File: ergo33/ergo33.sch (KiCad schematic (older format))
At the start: 112 parts, among them SW1 SW_Push, SW46 Rotary_Encoder_Switch, U1 ATmega32U4-AU, U2 USBLC6-2SC6, Y1 16MHz

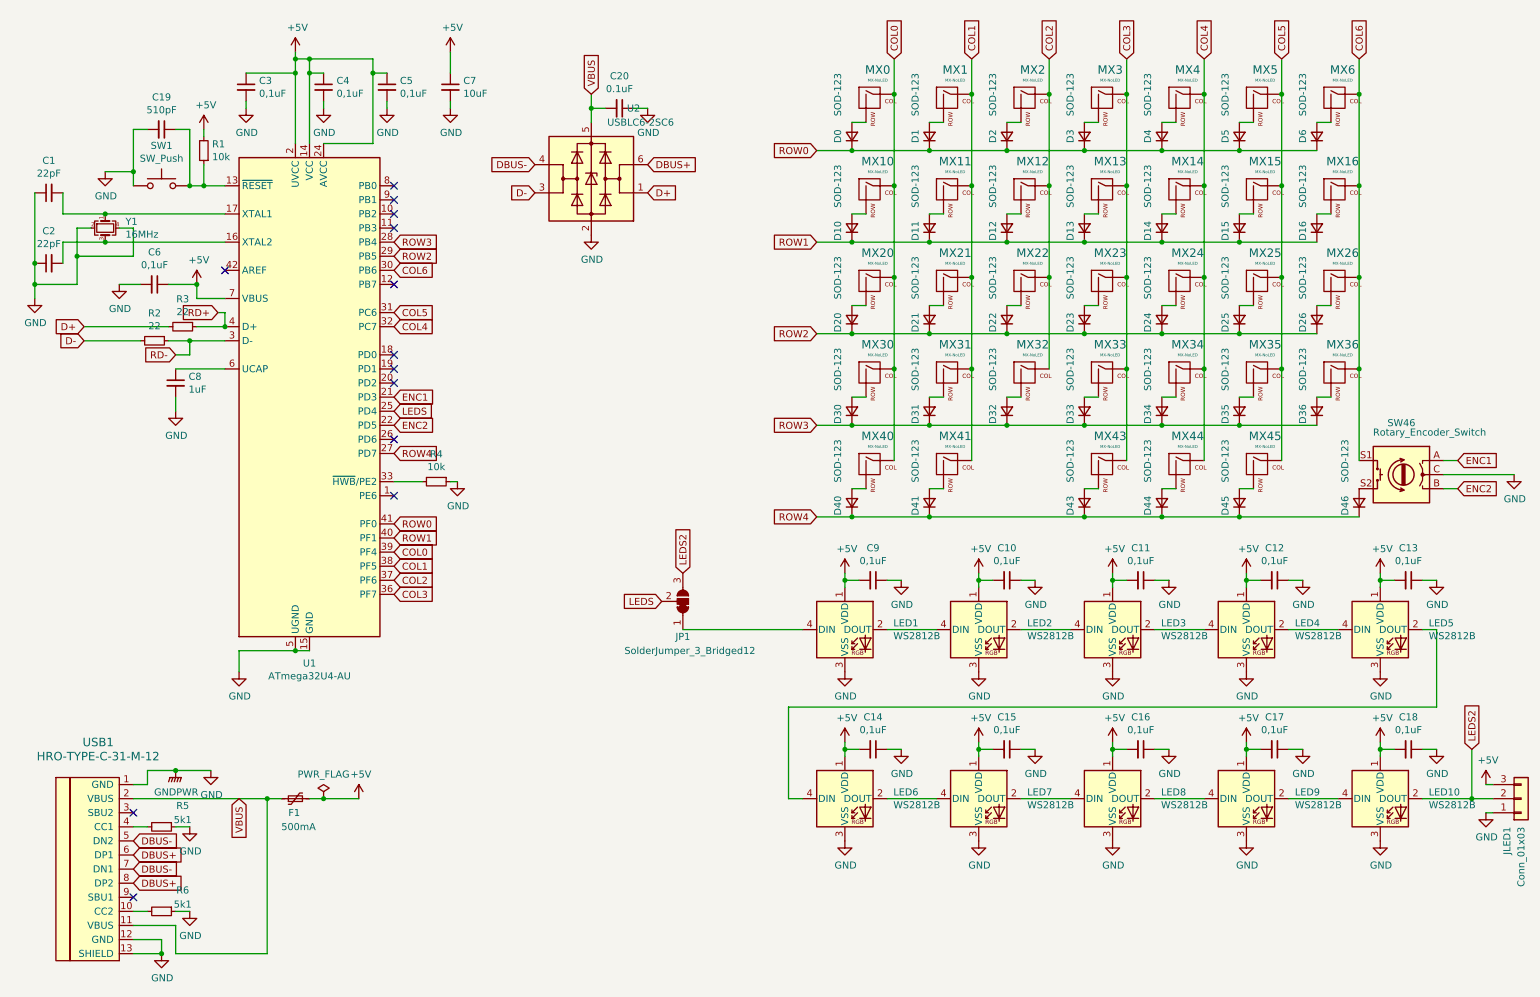
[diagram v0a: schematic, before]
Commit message: Change a few cap values
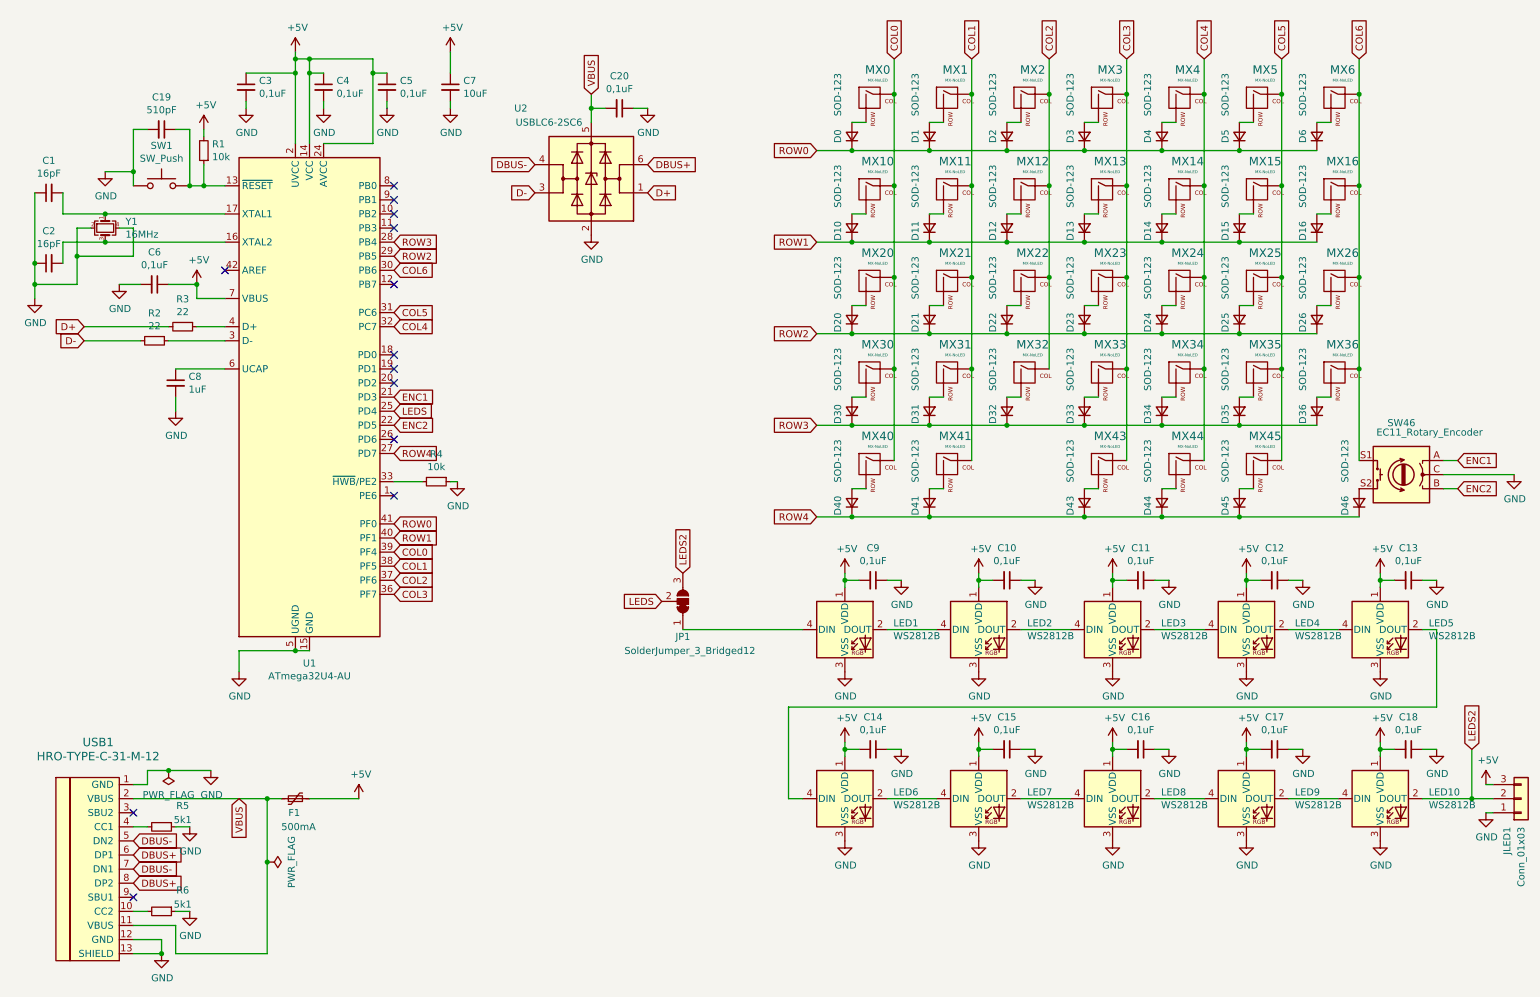
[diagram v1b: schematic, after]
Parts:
- C1, C2: value 22pF -> 16pF
- C20: value 0.1uF -> 0,1uF
- F1: Component (none) -> Littelfuse 1206L050/15
- MX0: Component (none) -> Kailh 1511 PCB socket
- SW46: value Rotary_Encoder_Switch -> EC11_Rotary_Encoder
- Y1: Component (none) -> DSX321G
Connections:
- net RD+: no longer names the net of R3.1, U1.4 (D+)
- net RD-: no longer names the net of R2.1, U1.3 (D-)
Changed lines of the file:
@@
 F 2 "Crystal:Crystal_SMD_3225-4Pin_3.2x2.5mm_HandSoldering" H 1100 2000 50  0001 C CNN
 F 3 "~" H 1100 2000 50  0001 C CNN
+F 4 "DSX321G" V 1100 2000 50  0001 C CNN "Component"
 	1    1100 2000
 	0    1    1    0
@@
 P 700 1750
 F 0 "C1" V 929 1750 50  0000 C CNN
-F 1 "22pF" V 838 1750 50  0000 C CNN
+F 1 "16pF" V 838 1750 50  0000 C CNN
 F 2 "Capacitor_SMD:C_0805_2012Metric_Pad1.15x1.40mm_HandSolder" H 700 1750 50  0001 C CNN
 F 3 "~" H 700 1750 50  0001 C CNN
@@
 P 700 2250
 F 0 "C2" V 929 2250 50  0000 C CNN
-F 1 "22pF" V 838 2250 50  0000 C CNN
+F 1 "16pF" V 838 2250 50  0000 C CNN
 F 2 "Capacitor_SMD:C_0805_2012Metric_Pad1.15x1.40mm_HandSolder" H 700 2250 50  0001 C CNN
 F 3 "~" H 700 2250 50  0001 C CNN
@@
 P 10300 3750
 F 0 "SW46" H 10300 4117 50  0000 C CNN
-F 1 "Rotary_Encoder_Switch" H 10100 4050 50  0000 C CNN
+F 1 "EC11_Rotary_Encoder" H 10100 4050 50  0000 C CNN
 F 2 "Rotary_Encoder:RotaryEncoder_Alps_EC11E-Switch_Vertical_H20mm" H 10150 3910 50  0001 C CNN
 F 3 "~" H 10300 4010 50  0001 C CNN
@@
 F 2 "MX_Only:MXOnly-1U-Hotswap" H 5925 1075 60  0001 C CNN
 F 3 "" H 5925 1075 60  0001 C CNN
+F 4 "Kailh 1511 PCB socket" H 6550 1100 50  0001 C CNN "Component"
 	1    6550 1100
 	1    0    0    -1
@@
 Connection ~ 1300 1600
 $Comp
-L power:GND #PWR0115
-U 1 1 5F1E9593
-P 1850 5850
-F 0 "#PWR0115" H 1850 5600 50  0001 C CNN
-F 1 "GND" H 1855 5677 50  0000 C CNN
-F 2 "" H 1850 5850 50  0001 C CNN
-F 3 "" H 1850 5850 50  0001 C CNN
-	1    1850 5850
-	1    0    0    -1
-$EndComp
-$Comp
 L power:GND #PWR0116
 U 1 1 5F1FCB7B
@@
 Connection ~ 1500 7150
 $Comp
-L power:PWR_FLAG #FLG0101
-U 1 1 5F224DEB
-P 2650 6050
-F 0 "#FLG0101" H 2650 6125 50  0001 C CNN
-F 1 "PWR_FLAG" H 2650 6223 50  0000 C CNN
-F 2 "" H 2650 6050 50  0001 C CNN
-F 3 "~" H 2650 6050 50  0001 C CNN
-	1    2650 6050
-	1    0    0    -1
-$EndComp
-$Comp
-L Device:Polyfuse_Small F1
-U 1 1 5F2261DB
-P 2450 6050
-F 0 "F1" V 2350 6100 50  0000 R CNN
-F 1 "500mA" V 2250 6150 50  0000 R CNN
-F 2 "Fuse:Fuse_1206_3216Metric_Pad1.42x1.75mm_HandSolder" H 2500 5850 50  0001 L CNN
-F 3 "~" H 2450 6050 50  0001 C CNN
-	1    2450 6050
-	0    -1   -1   0
-$EndComp
-$Comp
 L power:+5V #PWR0117
 U 1 1 5F227AE1
@@
 Wire Wire Line
 	2250 6050 2350 6050
-Wire Wire Line
-	2550 6050 2650 6050
 Connection ~ 2250 6050
 $Comp
@@
 	1600 7150 2250 7150
 Wire Wire Line
-	2250 6050 2250 7150
-Wire Wire Line
-	1300 6050 2250 6050
+	2250 6050 2250 6500
 Wire Wire Line
 	1300 5950 1400 5950
@@
 P 4750 1150
 F 0 "C20" V 4521 1150 50  0000 C CNN
-F 1 "0.1uF" V 4612 1150 50  0000 C CNN
+F 1 "0,1uF" V 4612 1150 50  0000 C CNN
 F 2 "Capacitor_SMD:C_0805_2012Metric_Pad1.15x1.40mm_HandSolder" H 4750 1150 50  0001 C CNN
 F 3 "~" H 4750 1150 50  0001 C CNN
@@
 U 1 1 5F4FCCDF
 P 4550 1650
-F 0 "U2" H 4250 2150 50  0000 C CNN
-F 1 "USBLC6-2SC6" H 4200 2050 50  0000 C CNN
+F 0 "U2" H 5050 2150 50  0000 C CNN
+F 1 "USBLC6-2SC6" H 4850 2050 50  0000 C CNN
 F 2 "Package_TO_SOT_SMD:SOT-23-6_Handsoldering" H 4550 1150 50  0001 C CNN
 F 3 "https://www.st.com/resource/en/datasheet/usblc6-2.pdf" H 4750 2000 50  0001 C CNN
@@
 	10950 5950 10900 5950
 Wire Wire Line
-	2650 6050 2900 6050
-Connection ~ 2650 6050
-Wire Wire Line
-	1600 5850 1850 5850
-Wire Wire Line
-	1400 5850 1600 5850
-Connection ~ 1600 5850
-$Comp
-L power:GNDPWR #PWR0156
-U 1 1 5FF5CD6C
-P 1600 5850
-F 0 "#PWR0156" H 1600 5650 50  0001 C CNN
-F 1 "GNDPWR" H 1604 5696 50  0000 C CNN
-F 2 "" H 1600 5800 50  0001 C CNN
-F 3 "" H 1600 5800 50  0001 C CNN
-	1    1600 5850
-	1    0    0    -1
-$EndComp
-Wire Wire Line
 	2650 1150 2650 1100
 $Comp
@@
 	1    0    0    -1
 $EndComp
-Connection ~ 1950 2700
-Wire Wire Line
-	1950 2600 1950 2700
-Wire Wire Line
-	1900 2600 1950 2600
-Wire Wire Line
-	1700 2800 1950 2800
-Wire Wire Line
-	1550 2800 1700 2800
-Connection ~ 1700 2800
-Wire Wire Line
-	1700 2900 1700 2800
-Wire Wire Line
-	1600 2900 1700 2900
-Text GLabel 1600 2900 0    50   Input ~ 0
-RD-
-Text GLabel 1900 2600 0    50   Input ~ 0
-RD+
+Wire Wire Line
+	1550 2800 1950 2800
+Wire Wire Line
+	1400 5850 1550 5850
+$Comp
+L power:PWR_FLAG #FLG0101
+U 1 1 5F224DEB
+P 2250 6500
+F 0 "#FLG0101" H 2250 6575 50  0001 C CNN
+F 1 "PWR_FLAG" H 2250 6673 50  0000 C CNN
+F 2 "" H 2250 6500 50  0001 C CNN
+F 3 "~" H 2250 6500 50  0001 C CNN
+	1    2250 6500
+	0    1    1    0
+$EndComp
+Connection ~ 2250 6500
+$Comp
+L Device:Polyfuse_Small F1
+U 1 1 5F2261DB
+P 2450 6050
+F 0 "F1" V 2350 6100 50  0000 R CNN
+F 1 "500mA" V 2250 6150 50  0000 R CNN
+F 2 "Fuse:Fuse_1206_3216Metric_Pad1.42x1.75mm_HandSolder" H 2500 5850 50  0001 L CNN
+F 3 "~" H 2450 6050 50  0001 C CNN
+F 4 "Littelfuse 1206L050/15" V 2450 6050 50  0001 C CNN "Component"
+	1    2450 6050
+	0    -1   -1   0
+$EndComp
+Wire Wire Line
+	2250 6500 2250 7150
+Wire Wire Line
+	2550 6050 2900 6050
+Wire Wire Line
+	1300 6050 2250 6050
+$Comp
+L power:PWR_FLAG #FLG0102
+U 1 1 5F21496B
+P 1550 5850
+F 0 "#FLG0102" H 1550 5925 50  0001 C CNN
+F 1 "PWR_FLAG" H 1550 6023 50  0000 C CNN
+F 2 "" H 1550 5850 50  0001 C CNN
+F 3 "~" H 1550 5850 50  0001 C CNN
+	1    1550 5850
+	-1   0    0    1
+$EndComp
+$Comp
+L power:GND #PWR0115
+U 1 1 5F1E9593
+P 1850 5850
+F 0 "#PWR0115" H 1850 5600 50  0001 C CNN
+F 1 "GND" H 1855 5677 50  0000 C CNN
+F 2 "" H 1850 5850 50  0001 C CNN
+F 3 "" H 1850 5850 50  0001 C CNN
+	1    1850 5850
+	1    0    0    -1
+$EndComp
+Connection ~ 1550 5850
+Wire Wire Line
+	1550 5850 1850 5850
 $EndSCHEMATC

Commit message: Ergo33: rev2
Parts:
- added C3: 10uF, Capacitor_SMD:C_0805_2012Metric_Pad1.15x1.40mm_HandSolder, symbol Device:C_Small
- JP1: value SolderJumper_3_Bridged12 -> SolderJumper_3_Open; footprint Jumper:SolderJumper-3_P1.3mm_Bridged2Bar12_Pad1.0x1.5mm_NumberLabels -> Jumper:SolderJumper-3_P1.3mm_Open_Pad1.0x1.5mm_NumberLabels; symbol Jumper:SolderJumper_3_Bridged12 -> Jumper:SolderJumper_3_Open
- renumbered C20 to C1, C2 to C10, C19 to C11, C9 to C12, C10 to C13, C11 to C14, C12 to C15, C13 to C16, C14 to C17, C15 to C18, C16 to C19, C7 to C2, C17 to C20, C18 to C21, C3 to C4, C4 to C5, C5 to C6, C6 to C7, C1 to C9, R5 to R1, R6 to R2, R4 to R3, R3 to R4, R2 to R5, R1 to R6
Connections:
- net +5V: now also C3.1
- net GND: now also C3.2
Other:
- moved on the sheet: C1, U2
